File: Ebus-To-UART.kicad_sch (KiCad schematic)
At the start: 27 parts, among them Q1 BC817, Q2 BC817, Q3 BC817, U1 LM358DR, U2 FODM217C, U3 FODM217C

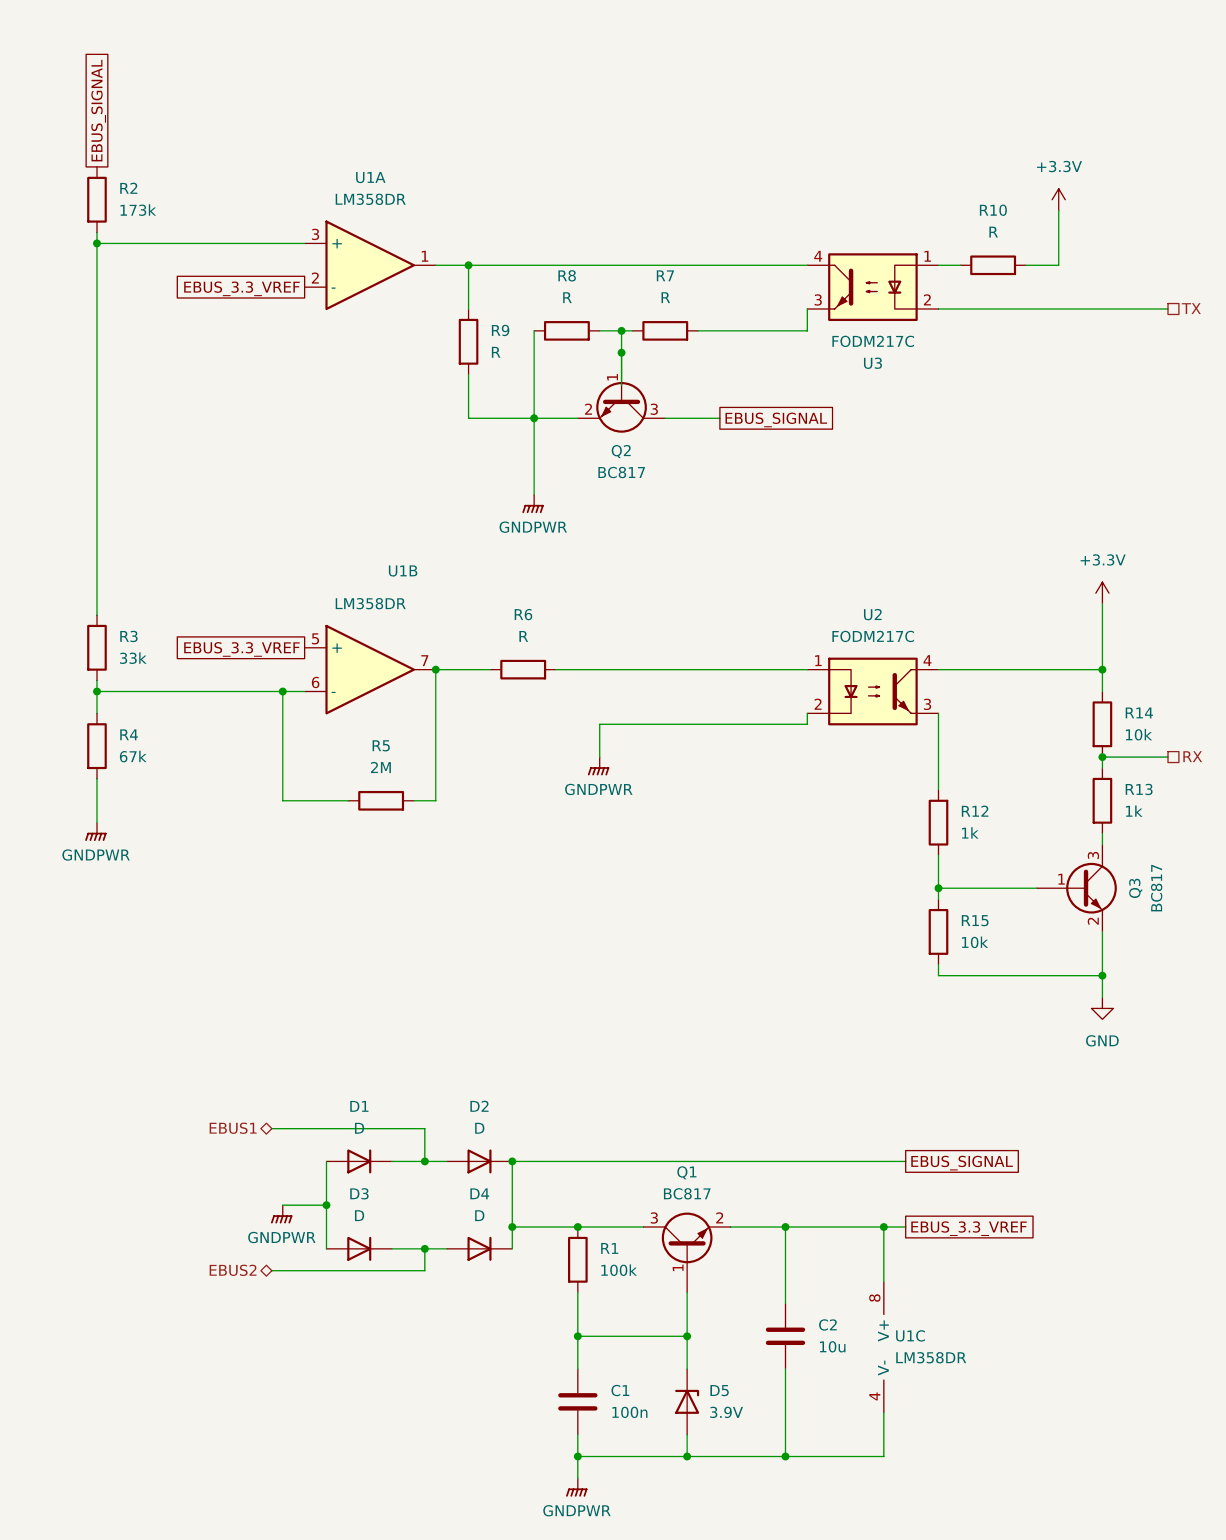
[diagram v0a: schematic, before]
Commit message: Updated adapter added SPI 2 Etherenet adapter
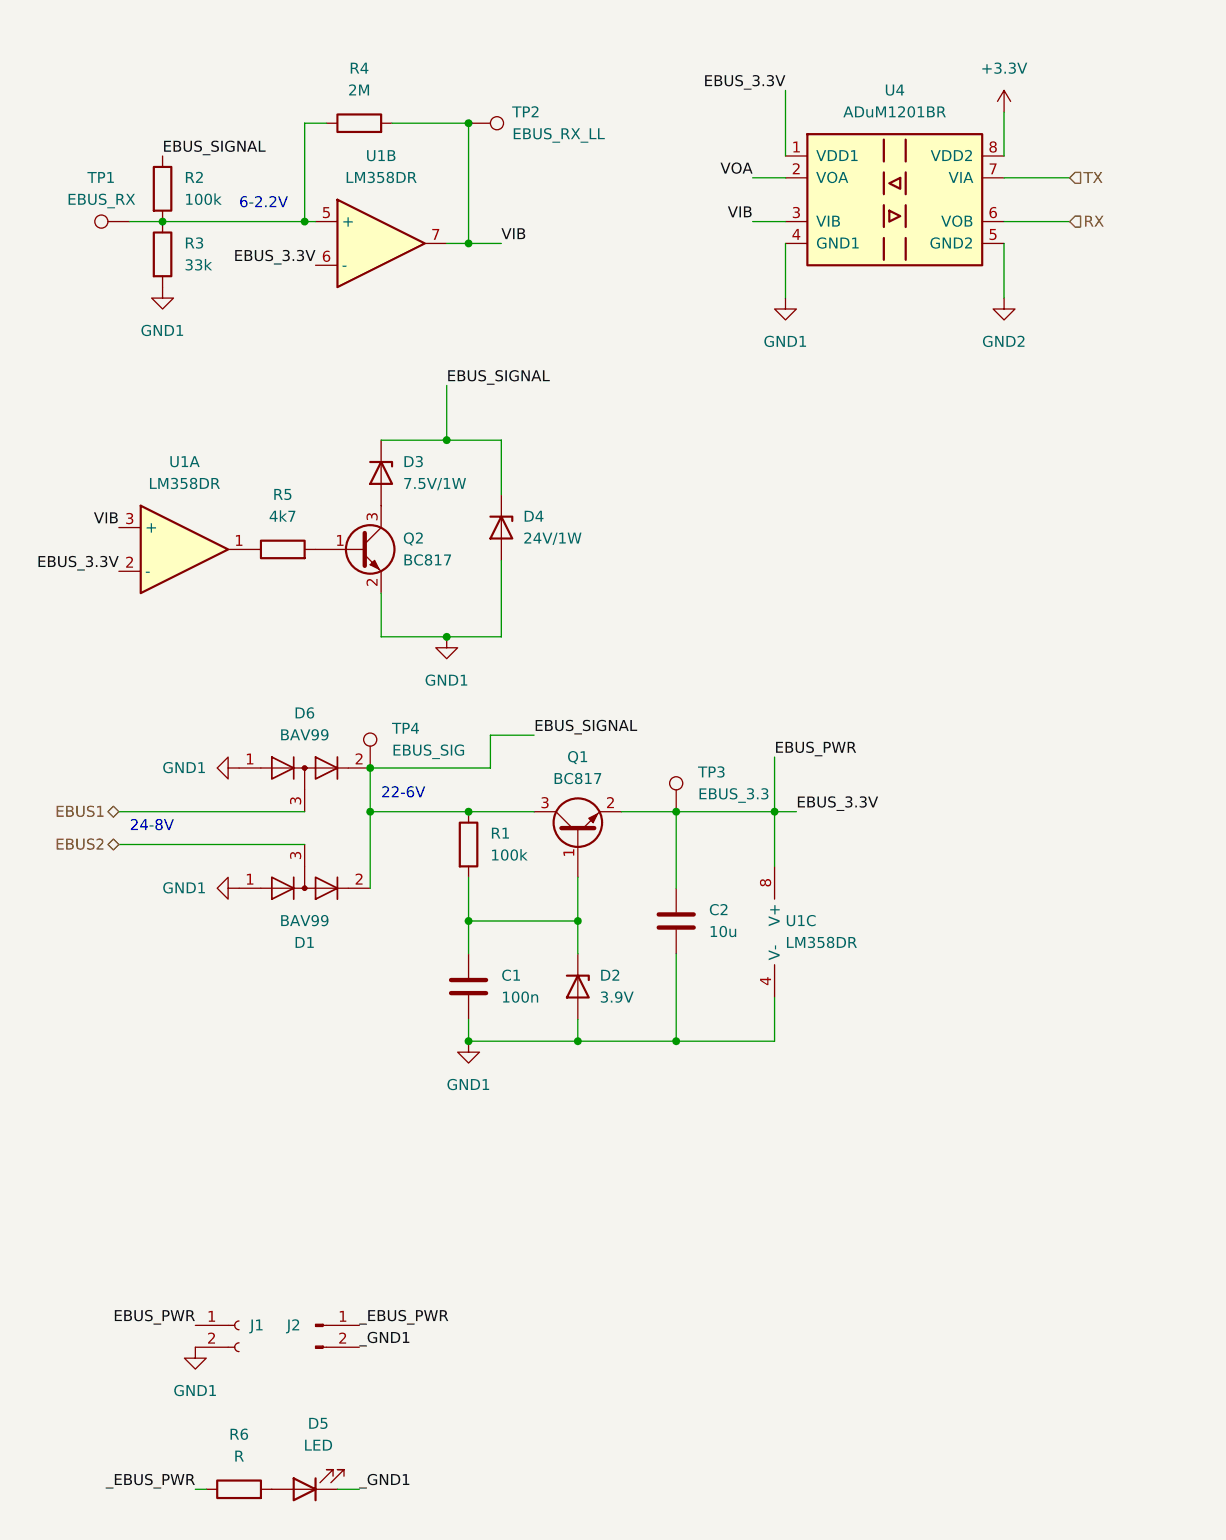
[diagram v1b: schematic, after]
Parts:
- removed D1, D2, D3, D4: D, Diode_SMD:D_MiniMELF, symbol Device:D
- removed D5: 3.9V, Package_TO_SOT_SMD:SOT-23, symbol Device:D_Zener
- removed Q3: BC817, Package_TO_SOT_SMD:SOT-23, symbol Transistor_BJT:BC817
- removed R10, R7, R8, R9: R, R_1206_3216Metric_Pad1.30x1.75mm_HandSolder, symbol Device:R
- removed R12, R13: 1k, R_1206_3216Metric_Pad1.30x1.75mm_HandSolder, symbol Device:R
- removed R14, R15: 10k, R_1206_3216Metric_Pad1.30x1.75mm_HandSolder, symbol Device:R
- removed U2, U3: FODM217C, Package_SO:SOP-4_4.4x2.6mm_P1.27mm, symbol Isolator:FODM217C
- added D1, D6: BAV99, Package_TO_SOT_SMD:SOT-23, symbol Diode:BAV99
- added D2: 3.9V, Diode_SMD:D_SOD-123, symbol Device:D_Zener
- added D3: 7.5V/1W, Diode_SMD:D_SOD-123, symbol Device:D_Zener
- added D4: 24V/1W, Diode_SMD:D_SOD-123, symbol Device:D_Zener
- added D5: LED, symbol Device:LED
- added J1: Conn_01x02_Socket, symbol Connector:Conn_01x02_Socket
- added J2: Conn_01x02_Pin, symbol Connector:Conn_01x02_Pin
- added TP1: EBUS_RX, symbol Connector:TestPoint
- added TP2: EBUS_RX_LL, symbol Connector:TestPoint
- added TP3: EBUS_3.3, symbol Connector:TestPoint
- added TP4: EBUS_SIG, symbol Connector:TestPoint
- added U4: ADuM1201BR, Package_SO:SOIC-8_3.9x4.9mm_P1.27mm, symbol Isolator:ADuM1201BR
- R2: value 173k -> 100k; footprint R_1206_3216Metric_Pad1.30x1.75mm_HandSolder -> (none)
- R3, R6: footprint R_1206_3216Metric_Pad1.30x1.75mm_HandSolder -> (none)
- R4: value 67k -> 2M; footprint R_1206_3216Metric_Pad1.30x1.75mm_HandSolder -> (none)
- R5: value 2M -> 4k7; footprint R_1206_3216Metric_Pad1.30x1.75mm_HandSolder -> (none)
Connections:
- net +3.3V: now also U4.8 (VDD2)
- net EBUS1: now also D6.3 (K)
- net EBUS2: now also D1.3 (K)
- net EBUS_SIGNAL: now also D1.2 (A), D3.1 (K), D4.1 (K), D6.2 (A), TP4.1; no longer Q2.3 (C)
- net RX: now also U4.6 (VOB)
- net TX: now also U4.7 (VIA)
- net at Q2.1 (B): now also R5.2
- net at R6.2: now also D5.2 (A)
- net at R2.2, R3.1: now also R4.1, U1.5 (+), TP1.1; no longer U1.3 (+)
- net at C1.1, Q1.1 (B), R1.2: now also D2.1 (K)
- net at U1.1: now also R5.1
- net EBUS_3.3_VREF renamed EBUS_3.3V
- net EBUS_3.3V: now also U1.6 (-), J1.1 (Pin_1), TP3.1, U4.1 (VDD1); no longer U1.5 (+)
- net GNDPWR renamed GND1
- net GND1: now also R3.2, D1.1 (K), D2.2 (A), D4.2 (A), D6.1 (K), J1.2 (Pin_2), U4.4 (GND1); no longer R4.2
- new net: D3.2 (A), Q2.3 (C)
- new net GND2: U4.5 (GND2)
- new net VIB: R4.2, TP2.1, U1.3 (+), U1.7, U4.3 (VIB)
- new net VOA: U4.2 (VOA)
- new net _EBUS_PWR: J2.1 (Pin_1), R6.1
- new net _GND1: D5.1 (K), J2.2 (Pin_2)
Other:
- note added: "22-6V"
- note added: "24-8V"
- note added: "6-2.2V"
- moved on the sheet: C1, C2, Q1, R1, U1A, U1B, U1C
